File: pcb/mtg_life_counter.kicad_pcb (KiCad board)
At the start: 2 copper layers, 167.6 x 101.6 mm, 84 parts, among them J1 USB_C_Receptacle_USB2.0, J2 ICSP, SW1 SW_SPST, SW2 SW_SPST, U1 ATmega328P-AU, U2 74HC595, U3 74HC595, U4 74HC595, U5 74HC595, U6 TPIC6B595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

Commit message: Fill some zones
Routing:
- net GND: vias 25 -> 27
- net (no net): vias 1 -> 0
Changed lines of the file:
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@@
     (thickness 1.6)
     (drawings 32)
-    (tracks 931)
+    (tracks 932)
     (zones 0)
     (modules 84)
@@
     (effects (font (size 2 2) (thickness 0.3)))
   )
-  (via (at 96.52 111.76) (size 0.8) (drill 0.4) (layers F.Cu B.Cu) (net 0))
   (segment (start 55.56 105.555) (end 55.93 105.925) (width 0.5) (layer F.Cu) (net 1))
   (segment (start 55.56 104.575) (end 55.56 105.555) (width 0.5) (layer F.Cu) (net 1))
@@
   (segment (start 120.65 123.19) (end 120.65 127.85) (width 0.5) (layer F.Cu) (net 1))
   (via (at 65.405 79.375) (size 0.8) (drill 0.4) (layers F.Cu B.Cu) (net 1))
+  (via (at 104.14 111.125) (size 0.8) (drill 0.4) (layers F.Cu B.Cu) (net 1))
+  (via (at 96.52 111.76) (size 0.8) (drill 0.4) (layers F.Cu B.Cu) (net 1))
   (via (at 96.52 106.68) (size 0.8) (drill 0.4) (layers F.Cu B.Cu) (net 2))
   (segment (start 94.728047 104.322361) (end 96.52 106.114314) (width 0.5) (layer F.Cu) (net 2))

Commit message: Add comments from design review
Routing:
- net GND: vias 27 -> 28
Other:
- board text added: "+5 polygon pour under U8 and arduino and caps"
- board text added: "1uF cap by the USB, after the switch"
- board text added: "Add teardropping on through hole pads"
- board text added: "Adjust traces by resonator to get copper pour up to pin 9 on uC"
- board text added: "Check for USB termination resistor requirements"
- board text added: "ESD protection diodes Clamping zener 20V+ varistor"
- board text added: "GROUND STICTICHIN!!!"
- board text added: "Increase power trace width"
- board text added: "Look for dangly bits on the pours"
- board text added: "add some DNP caps + resistors on clk and latch lines connect them roughly in order of the serial link close the C"
- board text added: "bigger exposed copper on ground lugs"
- board text added: "double up traces under usb"
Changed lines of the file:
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@@
-(kicad_pcb (version 20171130) (host pcbnew "(5.1.4)-1")
+(kicad_pcb (version 20171130) (host pcbnew "(5.1.5)-3")
   (general
     (thickness 1.6)
-    (drawings 32)
-    (tracks 932)
+    (drawings 44)
+    (tracks 933)
     (zones 0)
     (modules 84)
@@
     )
   )
+  (gr_text "Look for dangly bits on the pours\n" (at 97.79 172.72) (layer Cmts.User)
+    (effects (font (size 1.5 1.5) (thickness 0.3)))
+  )
+  (gr_text "Add teardropping on through hole pads" (at 96.52 160.655) (layer Cmts.User)
+    (effects (font (size 1.5 1.5) (thickness 0.3)))
+  )
+  (gr_text "GROUND STICTICHIN!!!" (at 239.395 136.525) (layer Cmts.User)
+    (effects (font (size 1.27 1.27) (thickness 0.15)))
+  )
+  (gr_text "1uF cap by the USB, after the switch" (at 31.75 146.685) (layer Cmts.User)
+    (effects (font (size 1 1) (thickness 0.15)))
+  )
+  (gr_text "add some DNP caps + resistors on clk and latch lines\nconnect them roughly in order of the serial link\nclose the C" (at 29.21 139.7) (layer Cmts.User)
+    (effects (font (size 1 1) (thickness 0.15)))
+  )
+  (gr_text "Adjust traces by resonator to get copper pour up to pin 9 on uC\n" (at 27.305 133.985) (layer Cmts.User)
+    (effects (font (size 1 1) (thickness 0.15)))
+  )
+  (gr_text "double up traces under usb" (at 10.16 109.855) (layer Cmts.User)
+    (effects (font (size 1.5 1.5) (thickness 0.3)))
+  )
+  (gr_text "+5 polygon pour under U8 and arduino and caps" (at 37.465 127) (layer Cmts.User)
+    (effects (font (size 1.5 1.5) (thickness 0.3)))
+  )
+  (gr_text "Increase power trace width" (at 27.94 120.015) (layer Cmts.User)
+    (effects (font (size 1.5 1.5) (thickness 0.3)))
+  )
+  (gr_text "ESD protection diodes\nClamping zener\n20V+ varistor" (at 47.625 111.76) (layer Cmts.User)
+    (effects (font (size 1.5 1.5) (thickness 0.3)))
+  )
+  (gr_text "Check for USB termination resistor requirements" (at 24.765 98.425) (layer Cmts.User)
+    (effects (font (size 1.5 1.5) (thickness 0.3)))
+  )
+  (gr_text "bigger exposed copper on ground lugs" (at 28.575 89.535) (layer Cmts.User)
+    (effects (font (size 1.5 1.5) (thickness 0.3)))
+  )
   (gr_text "TODO\n- Verify 7seg footprint\n- Verify TPIC footprint\n- Cosmetics\n- Check USB pin pitch\n- SMD LED version" (at 227.965 73.025) (layer Cmts.User)
     (effects (font (size 1.5 1.5) (thickness 0.3)) (justify left))
@@
   (via (at 104.14 111.125) (size 0.8) (drill 0.4) (layers F.Cu B.Cu) (net 1))
   (via (at 96.52 111.76) (size 0.8) (drill 0.4) (layers F.Cu B.Cu) (net 1))
+  (via (at 136.525 127) (size 0.8) (drill 0.4) (layers F.Cu B.Cu) (net 1))
   (via (at 96.52 106.68) (size 0.8) (drill 0.4) (layers F.Cu B.Cu) (net 2))
   (segment (start 94.728047 104.322361) (end 96.52 106.114314) (width 0.5) (layer F.Cu) (net 2))

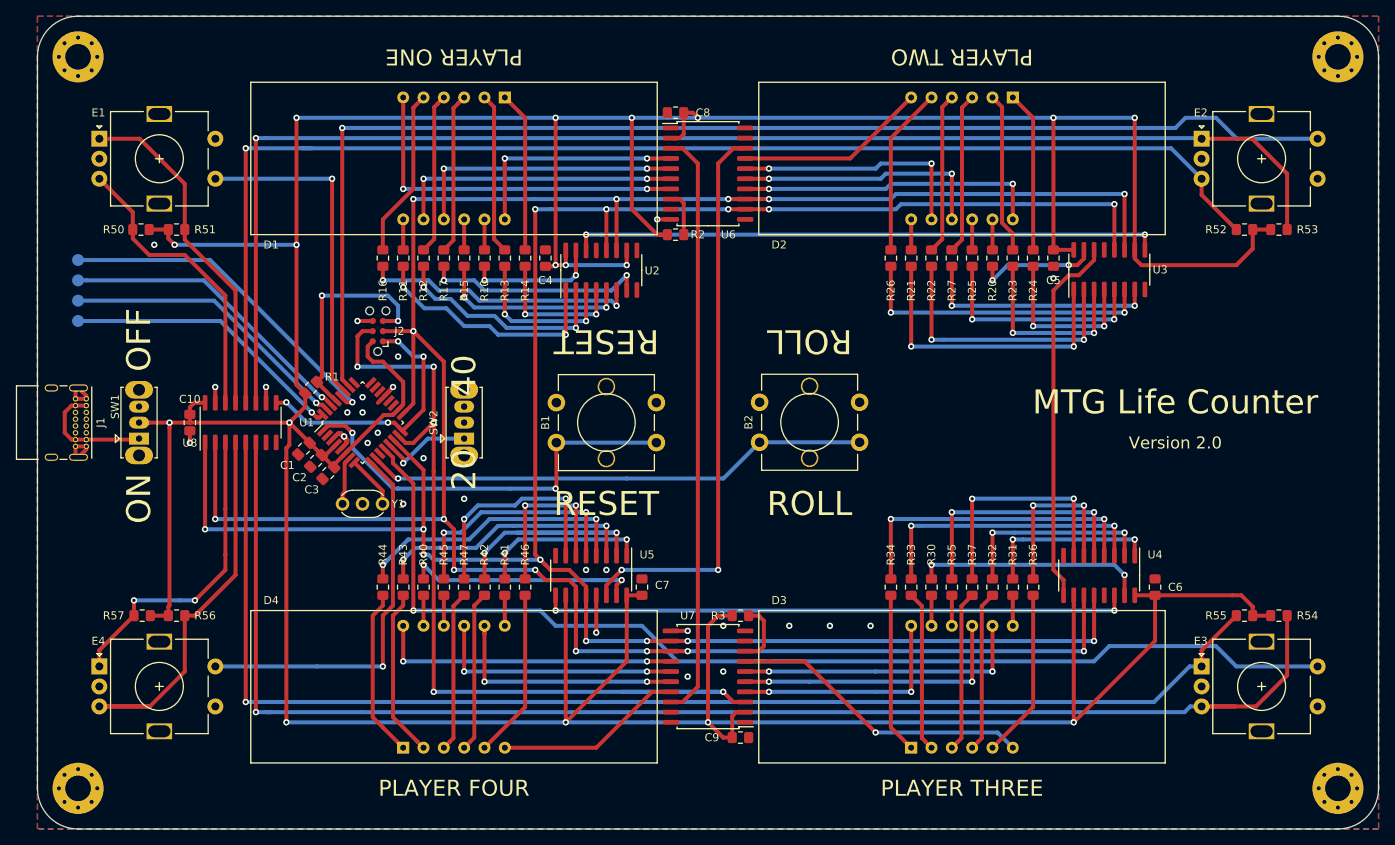
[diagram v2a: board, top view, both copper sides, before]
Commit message: Switch to SMD 7segs
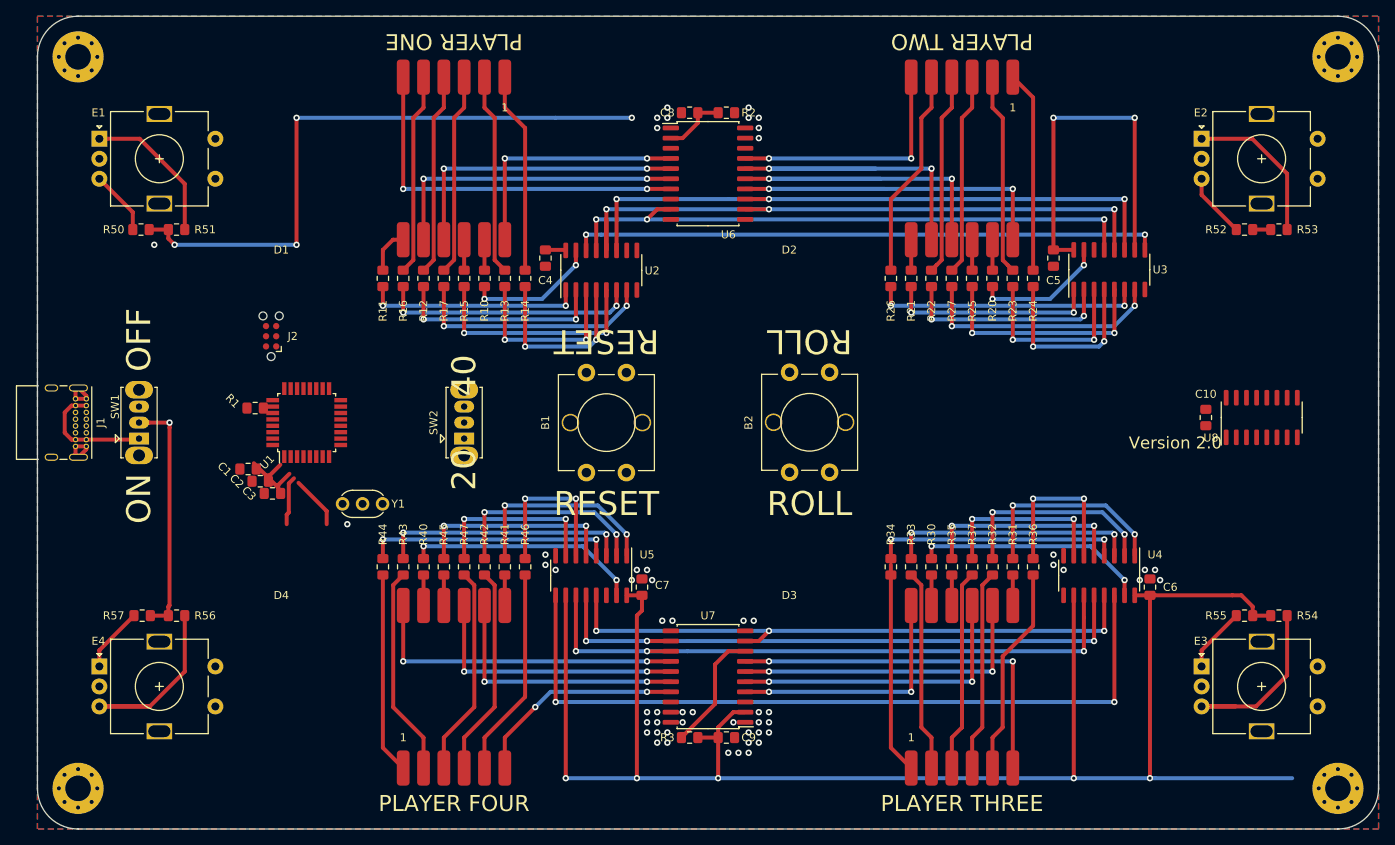
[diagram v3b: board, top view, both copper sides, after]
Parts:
- removed TP1: TX, TestPoint:TestPoint_Pad_D1.5mm
- removed TP2: RX, TestPoint:TestPoint_Pad_D1.5mm
- removed TP3: INT0, TestPoint:TestPoint_Pad_D1.5mm
- removed TP4: Debug, TestPoint:TestPoint_Pad_D1.5mm
- C4, C5, C6, C7, C8, C9: value 0.1uF -> 1uF
- D1: value KW4-566CVB RED -> KW4-S561CxB RED SMD; footprint mtg_life_counter:KW4-566xxB_THT -> mtg_life_counter:KW4-S561xxB_SMD
- D2: value KW4-566CVB GREEN -> KW4-S561CxB GREEN SMD; footprint mtg_life_counter:KW4-566xxB_THT -> mtg_life_counter:KW4-S561xxB_SMD
- D3: value KW4-566CVB YELLOW -> KW4-S561CxB YELLOW SMD; footprint mtg_life_counter:KW4-566xxB_THT -> mtg_life_counter:KW4-S561xxB_SMD
- D4: value KW4-566CVB BLUE -> KW4-S561CxB BLUE SMD; footprint mtg_life_counter:KW4-566xxB_THT -> mtg_life_counter:KW4-S561xxB_SMD
- moved U8 127.6 mm to (203.8, 101.0)
- moved C10 127.0 mm to (196.8, 101.0)
- moved R3 16.5 mm to (132.3, 141.0), turned to 0 degrees
- moved R2 16.5 mm to (136.9, 62.9)
- moved J2 13.4 mm to (80.0, 90.8)
- moved D4 9.92 mm to (102.9, 134.6), turned to 0 degrees
- moved D3 9.92 mm to (166.4, 134.6), turned to 0 degrees
- moved D1 9.92 mm to (102.9, 68.6), turned to 180 degrees
- moved D2 9.92 mm to (166.4, 68.6), turned to 180 degrees
- moved C1 7.43 mm to (77.1, 107.4), turned to 0 degrees
- moved R1 7.43 mm to (78.0, 99.8), turned to 0 degrees
- moved C2 7.43 mm to (78.7, 108.9), turned to 0 degrees
- moved C3 7.43 mm to (80.2, 110.5), turned to 0 degrees
- moved U1 6.98 mm to (84.5, 101.6), turned to 90 degrees
- moved R11 3.59 mm to (94.0, 83.6)
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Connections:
- U2 pad 13: GND -> /~ENABLE
- U3 pad 13: GND -> /~ENABLE
- U4 pad 13: GND -> /~ENABLE
- U5 pad 13: GND -> /~ENABLE
- U6 pad 9: GND -> /~ENABLE
- U7 pad 9: GND -> /~ENABLE
- U8 pad 15: GND -> /~ENABLE
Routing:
- net +5V: track 613.0 -> 393.5 mm, vias 17 -> 12
- net /E2_SW: track 156.3 -> 0.00 mm, vias 1 -> 0
- net /E2_DIR: track 162.3 -> 8.15 mm, vias 1 -> 0
- net /E3_CLK: track 161.9 -> 8.15 mm, vias 1 -> 0
- net /E3_DIR: track 176.9 -> 24.0 mm, vias 1 -> 0
- net /E2_CLK: track 170.8 -> 19.5 mm, vias 1 -> 0
- net /~ENABLE: track 0.00 -> 150.6 mm, vias 0 -> 6
- net /E3_SW: track 139.2 -> 0.00 mm, vias 1 -> 0
- net /SER_CLK: track 298.6 -> 159.7 mm, vias 14 -> 6
- net /SER_LATCH: track 279.7 -> 158.5 mm, vias 13 -> 6
- net /SER_MOSI: track 113.6 -> 0.00 mm, vias 5 -> 0
- net /SER_LINK_1: track 73.7 -> 0.00 mm
- net /SER_LINK_2: track 71.0 -> 0.00 mm, vias 2 -> 0
- net /ROLL_BTN: track 63.5 -> 0.00 mm, vias 1 -> 0
- net /RESET_BTN: track 52.1 -> 0.00 mm, vias 2 -> 0
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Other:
- board text removed: "MTG Life Counter"

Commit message: Complete layout. Use new USB-C connector
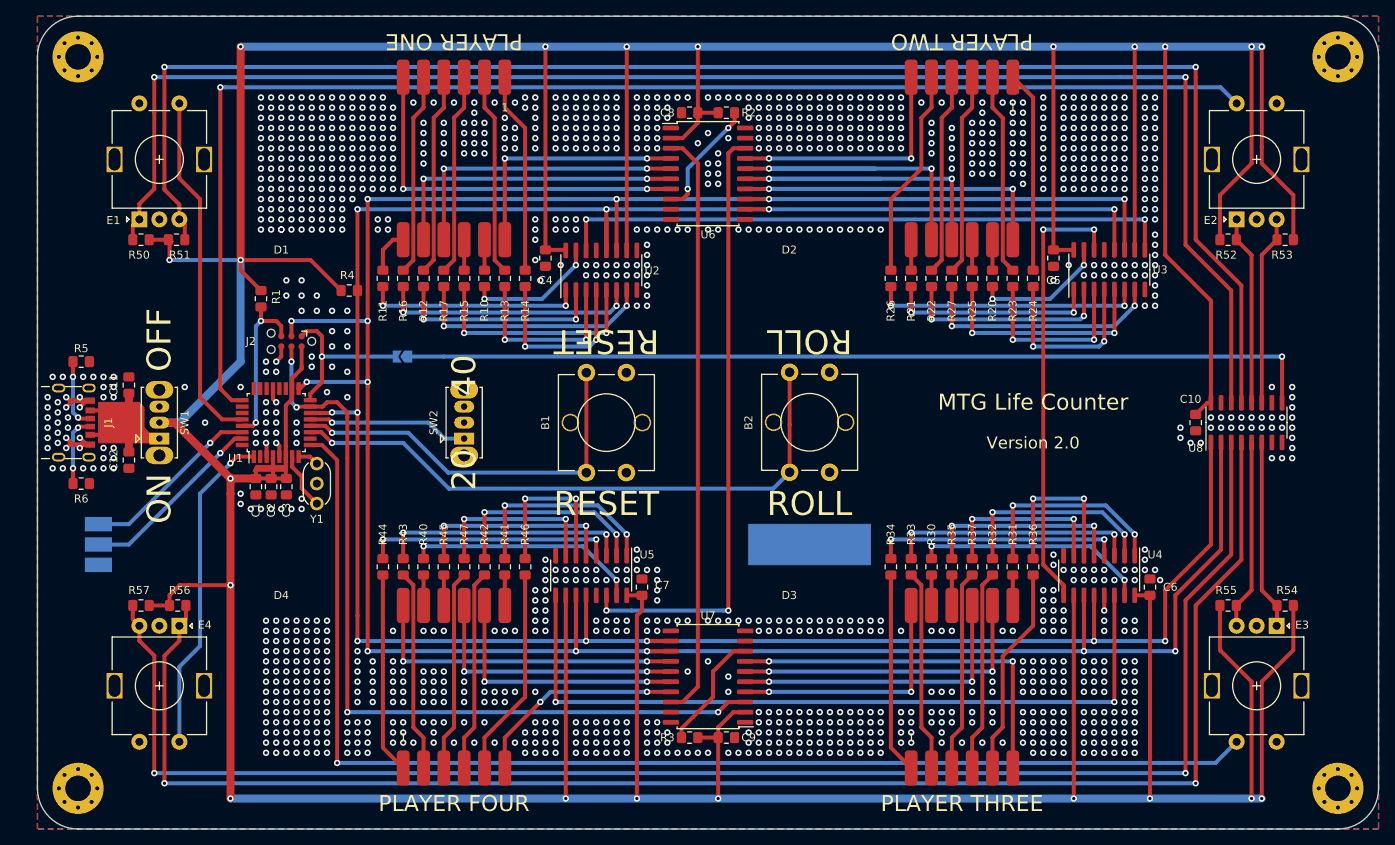
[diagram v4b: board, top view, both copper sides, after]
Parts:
- added C11: 1uF, Capacitor_SMD:C_0805_2012Metric_Pad1.15x1.40mm_HandSolder, F.Cu at (62.2, 96.9)
- added C12: 1uF, Capacitor_SMD:C_0805_2012Metric_Pad1.15x1.40mm_HandSolder, F.Cu at (62.2, 106.3)
- added JP1: Jumper_2_Open, Jumper:SolderJumper-2_P1.3mm_Open_TrianglePad1.0x1.5mm, B.Cu at (96.4, 93.3)
- added R4: 10k, Resistor_SMD:R_0805_2012Metric_Pad1.15x1.40mm_HandSolder, F.Cu at (89.8, 85.1)
- added R5: 5.1k, Resistor_SMD:R_0805_2012Metric_Pad1.15x1.40mm_HandSolder, F.Cu at (56.3, 94.0)
- added R6: 5.1k, Resistor_SMD:R_0805_2012Metric_Pad1.15x1.40mm_HandSolder, F.Cu at (56.3, 109.2)
- added TP1: TX, TestPoint:TestPoint_Keystone_5015_Micro-Minature, B.Cu at (58.4, 116.8)
- added TP2: RX, TestPoint:TestPoint_Keystone_5015_Micro-Minature, B.Cu at (58.4, 114.3)
- added TP3: GND, TestPoint:TestPoint_Keystone_5015_Micro-Minature, B.Cu at (58.4, 119.4)
- C4, C5, C6, C7, C8, C9: value 1uF -> 0.1uF
- J1: value USB_C_Receptacle_USB2.0 -> USB C 4907; footprint Connector_USB:USB_C_Receptacle_GCT_USB4085 -> mtg_life_counter:4907_USB_C_PowerOnly
- R1: value 1k -> 10k
- R20, R21, R22, R23, R24, R25, R26, R27: value 33 -> 10
- moved R1 13.7 mm to (78.7, 86.1), turned to 90 degrees
- moved E1 11.3 mm to (63.5, 76.2), turned to 90 degrees
- moved E4 11.2 mm to (68.5, 127.0), turned to 270 degrees
- moved E2 11.0 mm to (200.7, 76.2), turned to 90 degrees
- moved E3 10.7 mm to (205.7, 127.0), turned to 270 degrees
- moved J1 6.80 mm to (50.8, 101.6)
- moved U1 3.81 mm to (80.6, 101.6)
- moved Y1 3.22 mm to (85.7, 111.7), turned to 90 degrees
- moved J2 2.62 mm to (82.5, 91.4), turned to 180 degrees
- moved SW1 2.54 mm to (66.0, 103.6)
- moved C1 2.41 mm to (78.1, 109.6), turned to 90 degrees
- moved R55 2.41 mm to (199.6, 124.5), turned to 180 degrees
- moved R52 2.41 mm to (199.6, 78.7), turned to 180 degrees
- moved U8 2.01 mm to (201.9, 101.6)
- moved C3 1.93 mm to (81.9, 109.6), turned to 90 degrees
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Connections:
- net /D2(INT0) renamed Net-(U1-Pad32)
- E3 pad S1: GND -> /E3_SW
- E3 pad S2: /E3_SW -> GND
- H1 pad 1: GND -> Net-(H1-Pad1)
- H2 pad 1: GND -> Net-(H2-Pad1)
- H3 pad 1: GND -> Net-(H3-Pad1)
- H4 pad 1: GND -> Net-(H4-Pad1)
- J1 pad S1: GND -> (no net)
- R50 pad 1: /E1_DIR -> /E1_CLK
- R51 pad 1: /E1_CLK -> /E1_DIR
- R52 pad 1: /E2_DIR -> /E2_CLK
- R53 pad 1: /E2_CLK -> /E2_DIR
- R54 pad 1: /E3_DIR -> /E3_CLK
- R55 pad 1: /E3_CLK -> /E3_DIR
- R56 pad 1: /E4_DIR -> /E4_CLK
- R57 pad 1: /E4_CLK -> /E4_DIR
- U1 pad 1: /RESET_BTN -> /E4_SW
- U1 pad 10: /ROLL_BTN -> Net-(U1-Pad10)
- U1 pad 11: Net-(U1-Pad11) -> /ROLL_BTN
- U1 pad 12: /E3_SW -> /RESET_BTN
- U1 pad 25: Net-(U1-Pad25) -> /E2_SW
- U1 pad 26: /E2_SW -> Net-(U1-Pad26)
- U1 pad 27: /E1_SW -> Net-(U1-Pad27)
- U1 pad 28: /DEBUG_PIN -> /E1_SW
- U1 pad 9: /E4_SW -> /E3_SW
- U2 pad 13: /~ENABLE -> GND
- U3 pad 13: /~ENABLE -> GND
- U4 pad 13: /~ENABLE -> GND
- U5 pad 13: /~ENABLE -> GND
- U6 pad 9: /~ENABLE -> GND
- U7 pad 9: /~ENABLE -> GND
- U8 pad 11: /E2_CLK -> /E2_DIR
- U8 pad 12: /E2_DIR -> /E2_CLK
- U8 pad 13: /E1_CLK -> /E1_DIR
- U8 pad 14: /E1_DIR -> /E1_CLK
- U8 pad 15: /~ENABLE -> GND
- U8 pad 3: /E4_CLK -> /E4_DIR
- U8 pad 4: /E4_DIR -> /E4_CLK
- U8 pad 5: /E3_CLK -> /E3_DIR
- U8 pad 6: /E3_DIR -> /E3_CLK
- U8 pad 9: /SER_MISO -> /SR_OUT
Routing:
- net +5V: track 393.5 -> 918.9 mm, vias 12 -> 21
- net /E4_CLK: track 8.14 -> 197.2 mm, vias 0 -> 2
- net /E1_DIR: track 8.08 -> 195.9 mm, vias 0 -> 2
- net /E1_CLK: track 18.8 -> 193.4 mm, vias 0 -> 2
- net /SER_CLK: track 159.7 -> 334.1 mm, vias 6 -> 13
- net /E2_SW: track 0.00 -> 168.9 mm, vias 0 -> 1
- net /E4_DIR: track 25.9 -> 194.7 mm, vias 0 -> 2
- net /SER_LATCH: track 158.5 -> 314.2 mm, vias 6 -> 11
- net /E3_SW: track 0.00 -> 155.5 mm, vias 0 -> 1
- net /~ENABLE: track 150.6 -> 0.00 mm, vias 6 -> 0
- net /SR_OUT: track 0.00 -> 115.0 mm, vias 0 -> 1
- net /SER_MOSI: track 0.00 -> 102.7 mm, vias 0 -> 4
- net /SER_LINK_2: track 0.00 -> 76.7 mm, vias 0 -> 2
- net /ROLL_BTN: track 0.00 -> 76.2 mm, vias 0 -> 1
- net /SER_LINK_1: track 0.00 -> 73.7 mm
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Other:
- net class Power: trace_width 0.5 -> 1
- board text added: "JLCJLCJLCJLC"
- board text added: "MTG Life Counter"
- board text added: "Max Proskauer v2.0 Dec 2021 github.com/mprosk/mtg_life_counter"
- board text removed: "Max Proskauer v2.0 Oct 2020 github.com/mprosk/mtg_life_counter"

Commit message: Tweak encoder footprint. Add more via stitching
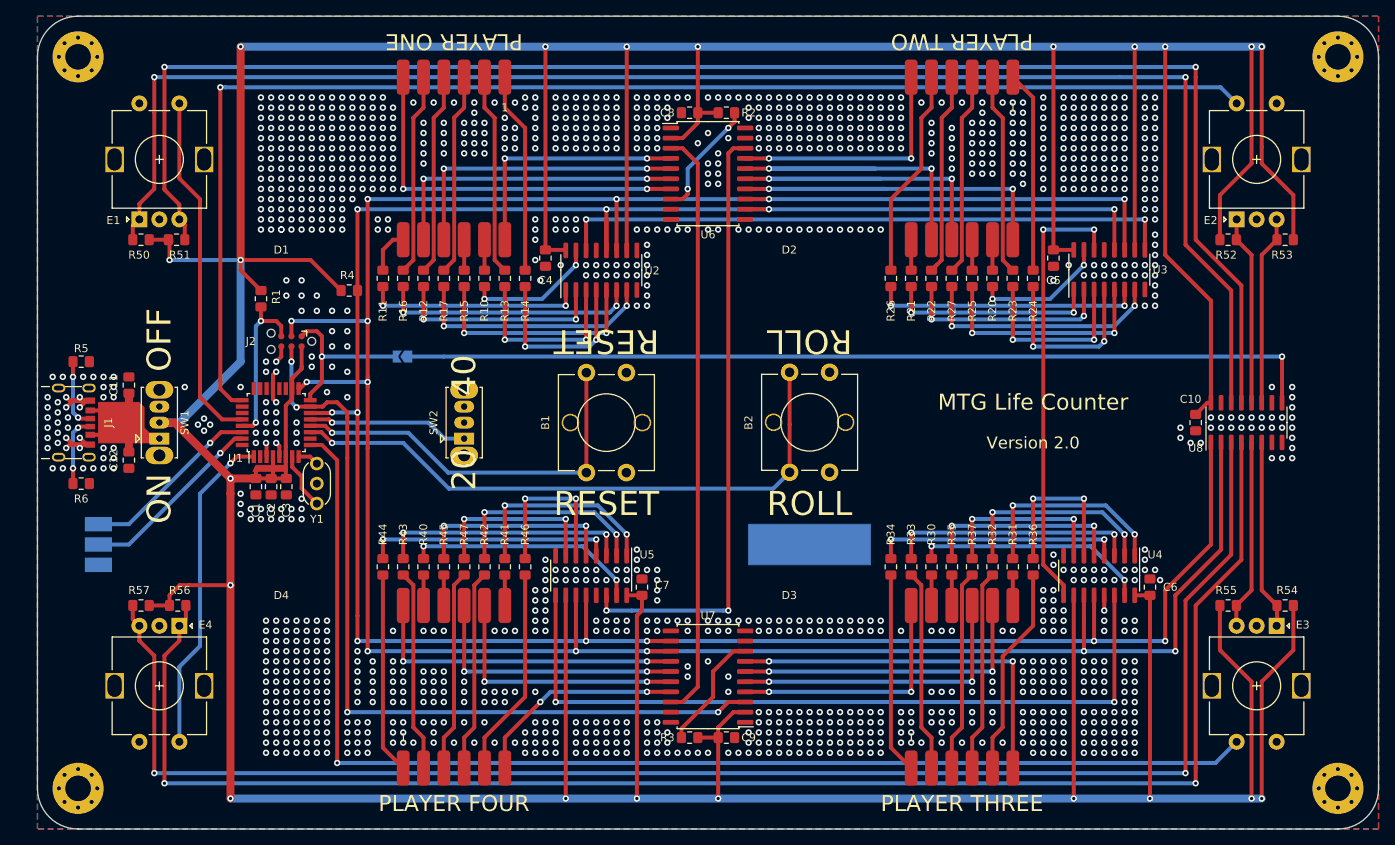
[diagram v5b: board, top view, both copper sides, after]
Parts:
- E1, E2, E3, E4: footprint Rotary_Encoder:RotaryEncoder_Alps_EC11E-Switch_Vertical_H20mm -> mtg_life_counter:TT_EN11-HSB
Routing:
- net GND: track 28.9 -> 31.2 mm, vias 1312 -> 1328
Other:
- board text added: "TODO - Verify encoder footprint (mounting points)"
- board text removed: "TODO - Verify 7seg footprint - Verify TPIC footprint - Cosmetics - Check USB pin pitch - SMD LED version"
